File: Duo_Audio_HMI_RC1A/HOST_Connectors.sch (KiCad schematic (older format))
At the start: 47 parts, among them P6 HEADER_8X2, U7 A20_ITEAD_CORE

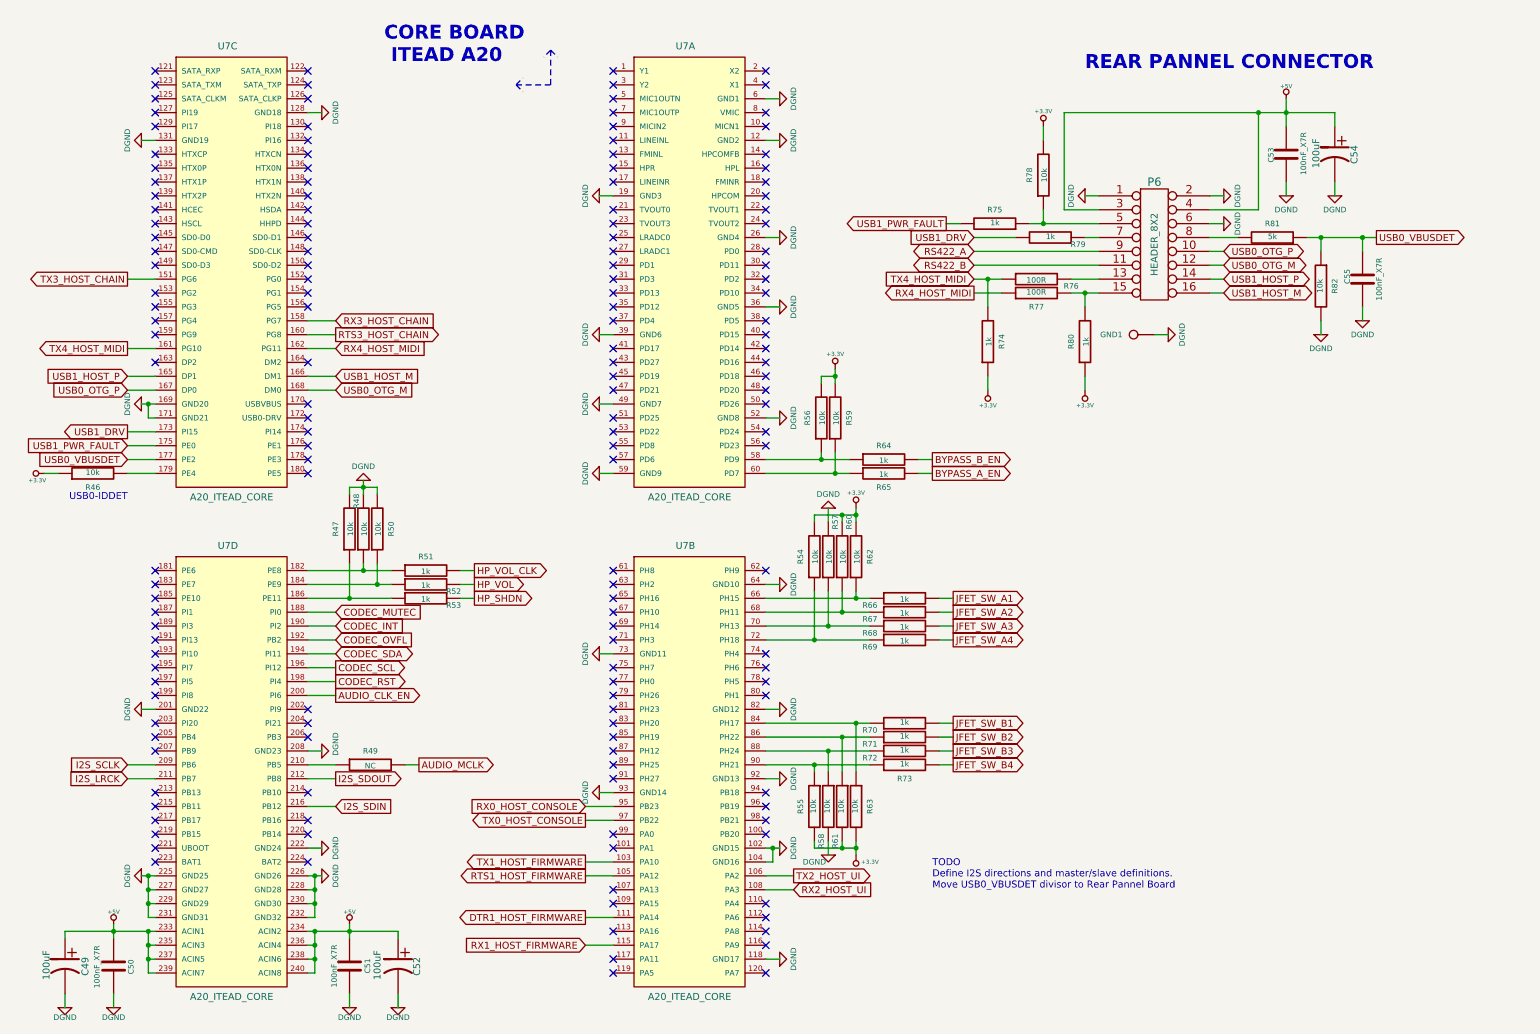
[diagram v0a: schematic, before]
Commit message: Implementing RCA1 schematic  modifications for new layout. Backup commit.
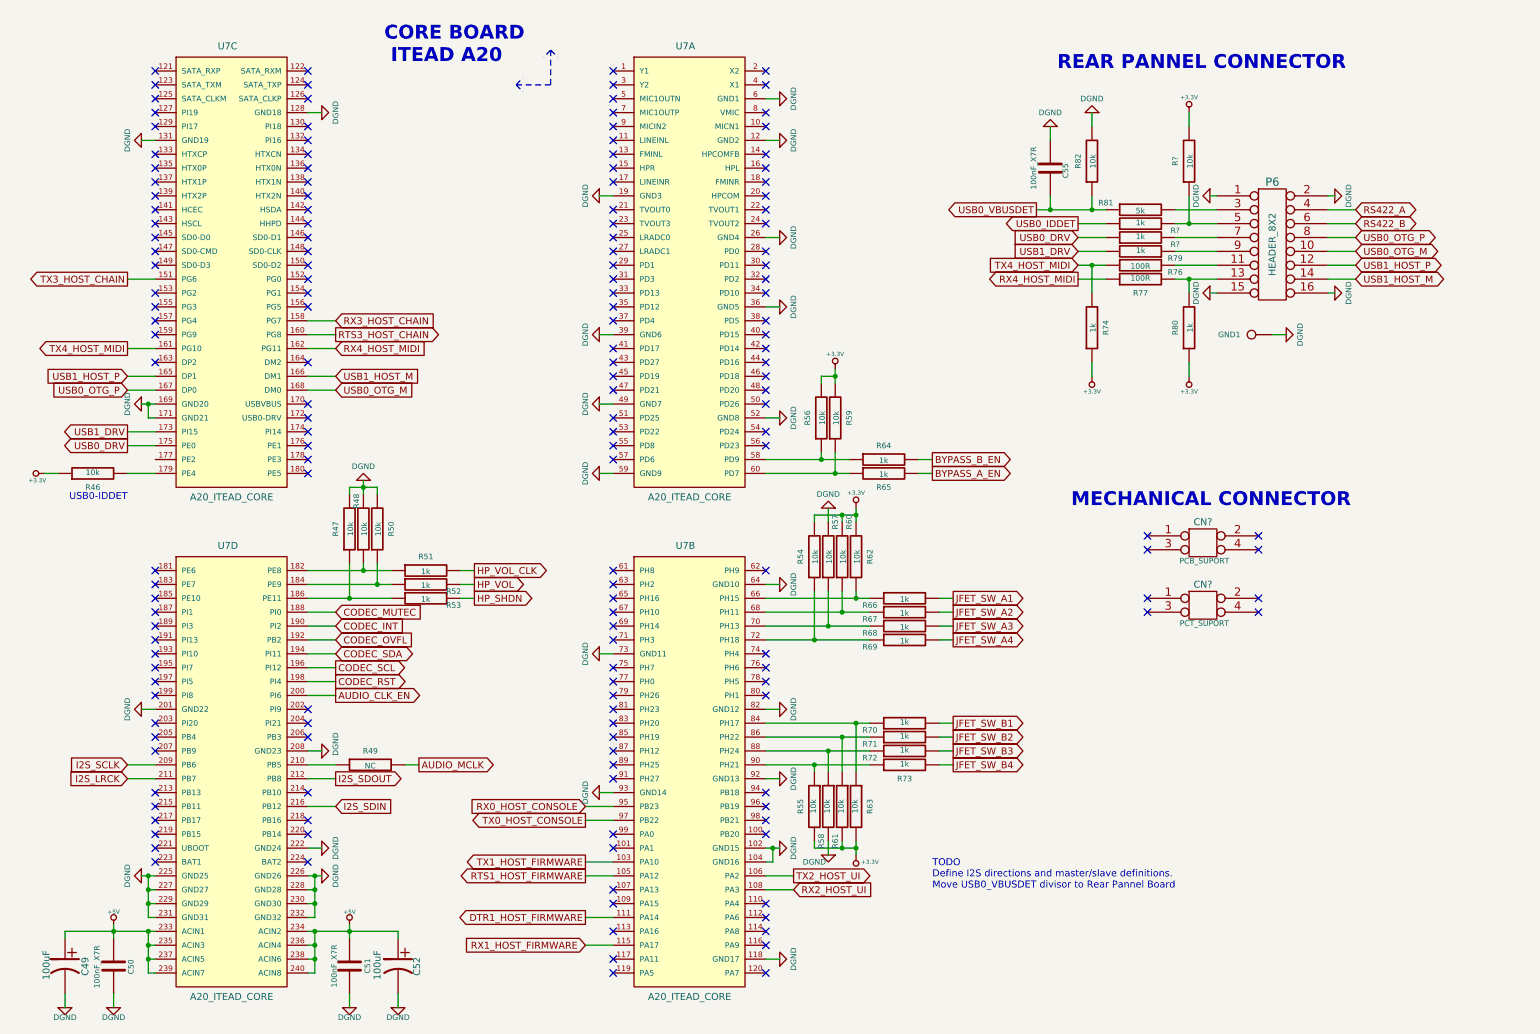
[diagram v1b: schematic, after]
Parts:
- removed C53: 100nF_X7R, SM0603, symbol C
- removed C54: 100uF, CAP_RAD_5MM, symbol CP1
- removed R75: 1k, SM0603, symbol R
- removed R78: 10k, SM0603, symbol R
- added CN?: PCB_SUPORT, symbol CONN_2X2
- added CN?: PCT_SUPORT, symbol CONN_2X2
- added R? (x2): 1k, SM0603, symbol R
- added R?: 10k, SM0603, symbol R
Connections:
- net +3.3V: now also R?.2
- net +5V: no longer P6.3, P6.4
- net DGND: now also P6.15, P6.16; no longer P6.6
- net RS422_A: now also P6.4; no longer P6.9
- net RS422_B: now also P6.6; no longer P6.11
- net USB0_OTG_M: now also P6.10; no longer P6.12
- net USB0_OTG_P: now also P6.8; no longer P6.10
- net USB0_VBUSDET: no longer U7.177 (PE2)
- net USB1_HOST_M: now also P6.14; no longer P6.16
- net USB1_HOST_P: now also P6.12; no longer P6.14
- net at R76.2: now also P6.11; no longer P6.13
- net at R77.2, R80.2: now also P6.13; no longer P6.15
- net at P6.5: now also R?.1, R?.2
- net at P6.7: now also R?.2; no longer R79.1
- net at R81.2: now also P6.3; no longer P6.8
- net USB1_PWR_FAULT renamed USB0_DRV
- net USB0_DRV: now also R?.1
- new net: P6.9, R79.1
- new net USB0_IDDET: R?.1
- no-connect marks 154 -> 162
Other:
- note added: "MECHANICAL CONNECTOR"
- moved on the sheet: C55, GND1, P6, R74, R76, R77, R79, R80, R81, R82

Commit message: Finished RCA1 schematic of the Baseboard and the Pannelboard with USB OTG. Board dimensions, most footprint attribution and major placement implemented in layout. Learning GIT!
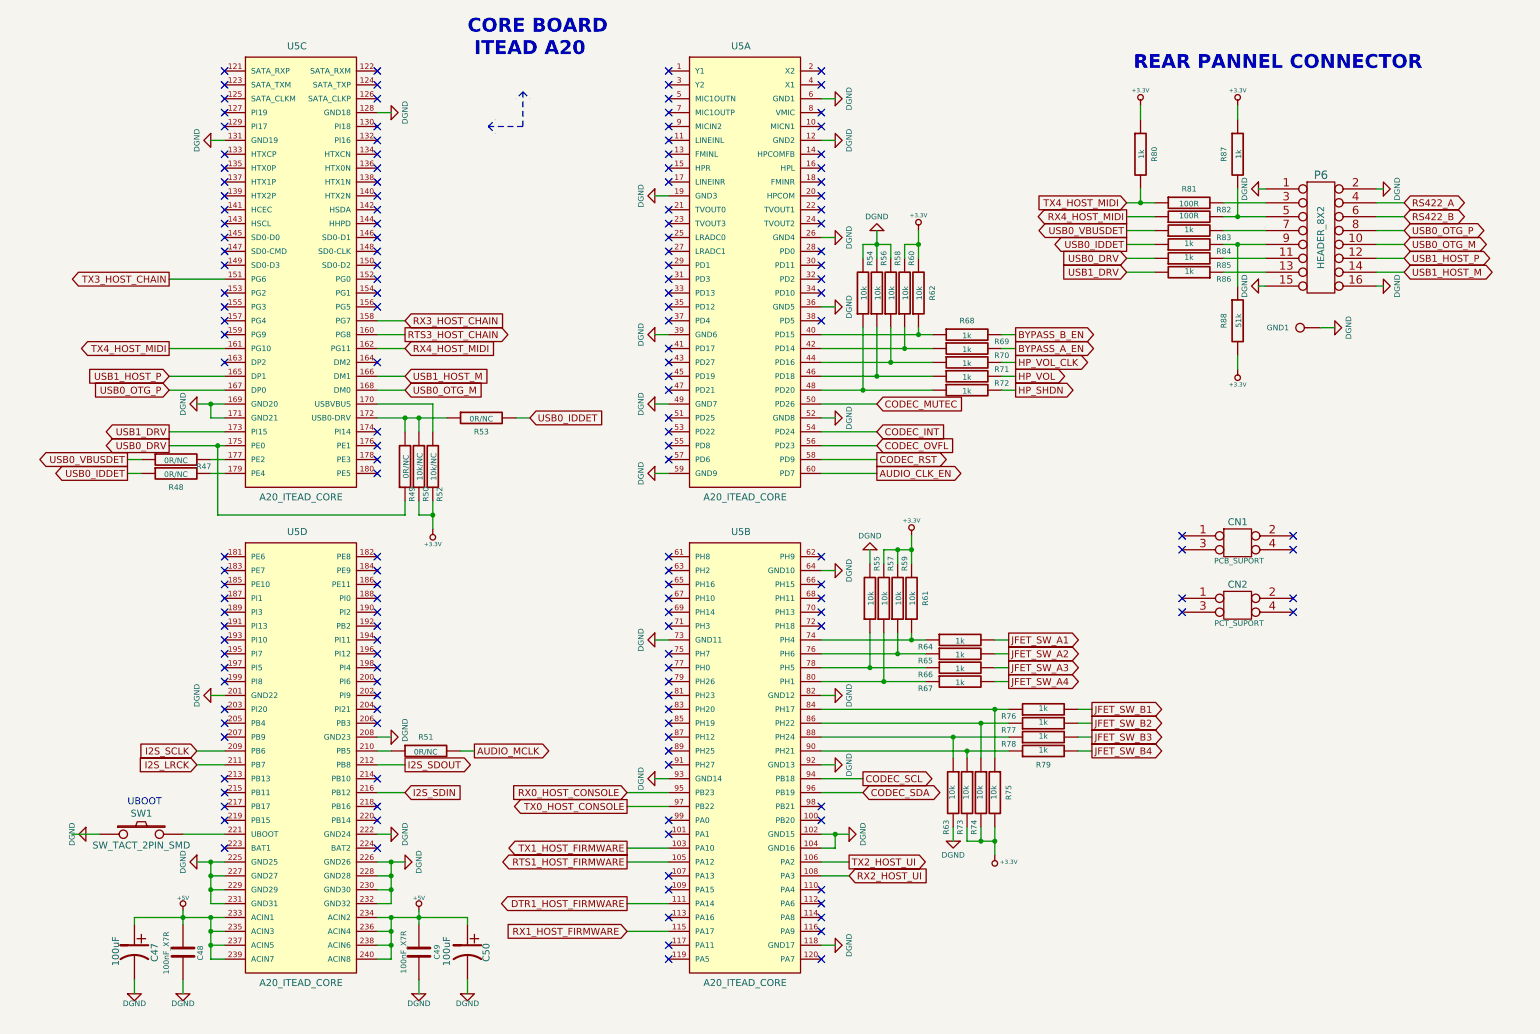
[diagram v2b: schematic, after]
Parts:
- removed C55: 100nF_X7R, SM0603, symbol C
- removed R46, R82: 10k, SM0603, symbol R
- removed R81: 5k, SM0603, symbol R
- added R47, R48, R49, R53: 0R/NC, SM0603, symbol R
- added R50, R52: 10k/NC, SM0603, symbol R
- added R83: 1k, SM0603, symbol R
- added SW1: SW_TACT_2PIN_SMD, SWITCH_SMD_FSMSM, symbol SW_PUSH
- CN1, CN2: renamed from CN?; footprint (none) -> PCB_SUPORT
- R51: renamed from R49; value NC -> 0R/NC
- R88: renamed from R?; value 10k -> 51k
- gave numbers to parts that had none: 2
- renumbered C49 to C47, C50 to C48, C51 to C49, C52 to C50, R47 to R54, R57 to R55, R48 to R56, R54 to R57, R50 to R58, R60 to R59, R56 to R60, R62 to R61, R59 to R62, R58 to R63, R66 to R64, R67 to R65, R68 to R66, R69 to R67, R64 to R68, R65 to R69, R51 to R70, R52 to R71, R53 to R72, R55 to R73, R61 to R74, R63 to R75, R70 to R76, R71 to R77, R72 to R78, R73 to R79, R74 to R80, R77 to R81, R76 to R82, R79 to R86, R80 to R87, U7 to U5
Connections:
- net +3.3V: now also R50.1, R52.1
- net AUDIO_CLK_EN: now also U5.60 (PD7); no longer U5.200 (PI6)
- net CODEC_INT: now also U5.54 (PD24); no longer U5.190 (PI2)
- net CODEC_MUTEC: now also U5.50 (PD26); no longer U5.188 (PI0)
- net CODEC_OVFL: now also U5.56 (PD23); no longer U5.192 (PB2)
- net CODEC_RST: now also U5.58 (PD9); no longer U5.198 (PI4)
- net CODEC_SCL: now also U5.94 (PB18); no longer U5.196 (PI12)
- net CODEC_SDA: now also U5.96 (PB19); no longer U5.194 (PI11)
- net RX4_HOST_MIDI: now also R82.1; no longer R81.1
- net TX4_HOST_MIDI: now also R81.1; no longer R82.1
- net USB0_DRV: now also R49.1
- net USB0_IDDET: now also R48.1, R53.2
- net USB0_VBUSDET: now also R47.1, R83.1
- net at P6.11: now also R85.2; no longer R82.2
- net at P6.3: now also R81.2
- net at R84.2, R88.1: now also P6.9; no longer P6.5
- net at P6.7: now also R83.2; no longer R85.2
- net at R86.1: now also P6.13; no longer P6.9
- net at R57.1, R67.1: now also U5.80 (PH1); no longer U5.72 (PH18)
- net at R55.1, R66.1: now also U5.78 (PH5); no longer U5.70 (PH13)
- net at R59.1, R65.1: now also U5.76 (PH6); no longer U5.68 (PH11)
- net at R61.1, R64.1: now also U5.74 (PH4); no longer U5.66 (PH15)
- net at R54.1, R72.1: now also U5.48 (PD20); no longer U5.186 (PE11)
- net at U5.221 (UBOOT): now also SW1.2
- net at U5.40 (PD15): now also R62.1, R68.1
- net at U5.42 (PD14): now also R60.1, R69.1
- net at U5.44 (PD16): now also R58.1, R70.1
- net at U5.46 (PD18): now also R56.1, R71.1
- net at U5.170 (USBVBUS): now also R52.2
- net at U5.172 (USB0-DRV): now also R49.2, R50.2, R53.1
- net at U5.177 (PE2): now also R47.2
- net at U5.179 (PE4): now also R48.2
- new net: P6.5, R82.2, R87.2
- now unconnected: U5.182 (PE8), U5.184 (PE9)
- no-connect marks 162 -> 159
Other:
- note added: "UBOOT"
- note removed: "MECHANICAL CONNECTOR"
- note removed: "TODO\nDefine I2S directions and master/slave definitions.\nMove USB0_VBUSDET divisor to Rear Pannel Board"
- note removed: "USB0-IDDET"
- moved on the sheet: C47, C48, C49, C50, CN1, CN2, GND1, P6, R51, R54, R55, R56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

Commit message: Major changes on hardware architecture. Migrating to a HMI separated board. HMI schematic finalized.
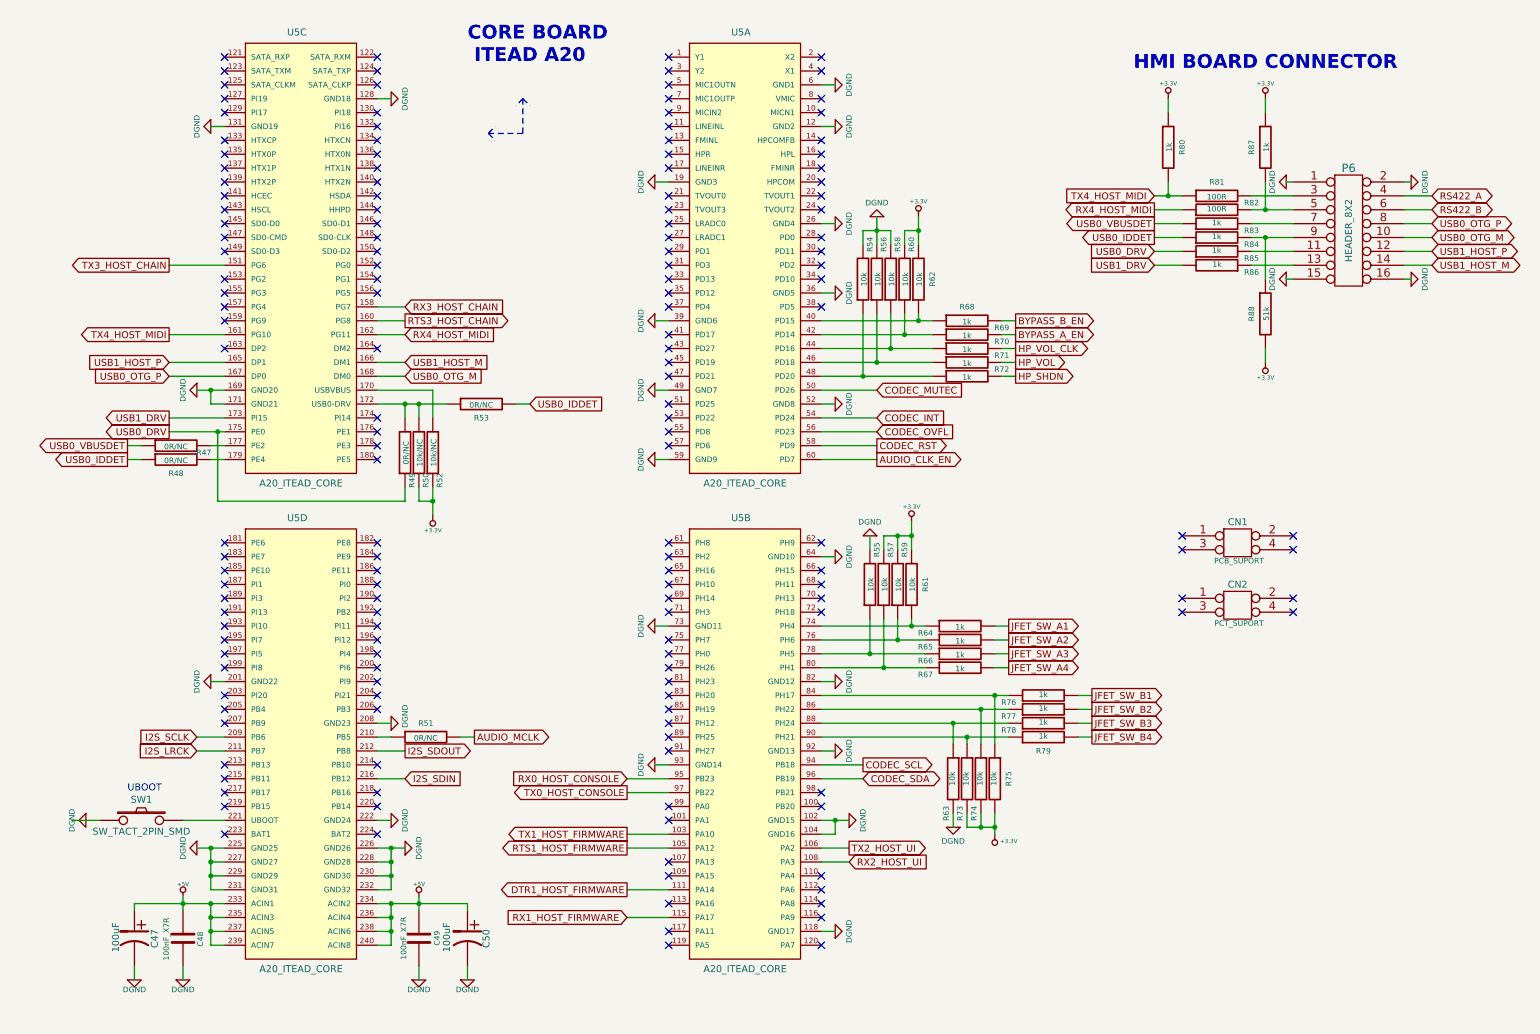
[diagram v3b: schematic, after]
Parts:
- removed GND1: CONN_1, symbol CONN_1
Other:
- note added: "HMI BOARD CONNECTOR"
- note removed: "REAR PANNEL CONNECTOR"
- moved on the sheet: C47, C48, C49, C50, P6, R47, R48, R49, R50, R51, R52, R53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
